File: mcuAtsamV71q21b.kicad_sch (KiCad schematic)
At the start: 29 parts, among them J2 TC2050, U1 ATSAMV71Q21B-A, Y2 12MHz, Y3 CM8V-T1A0.332.768KHZ4PF+_-20P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

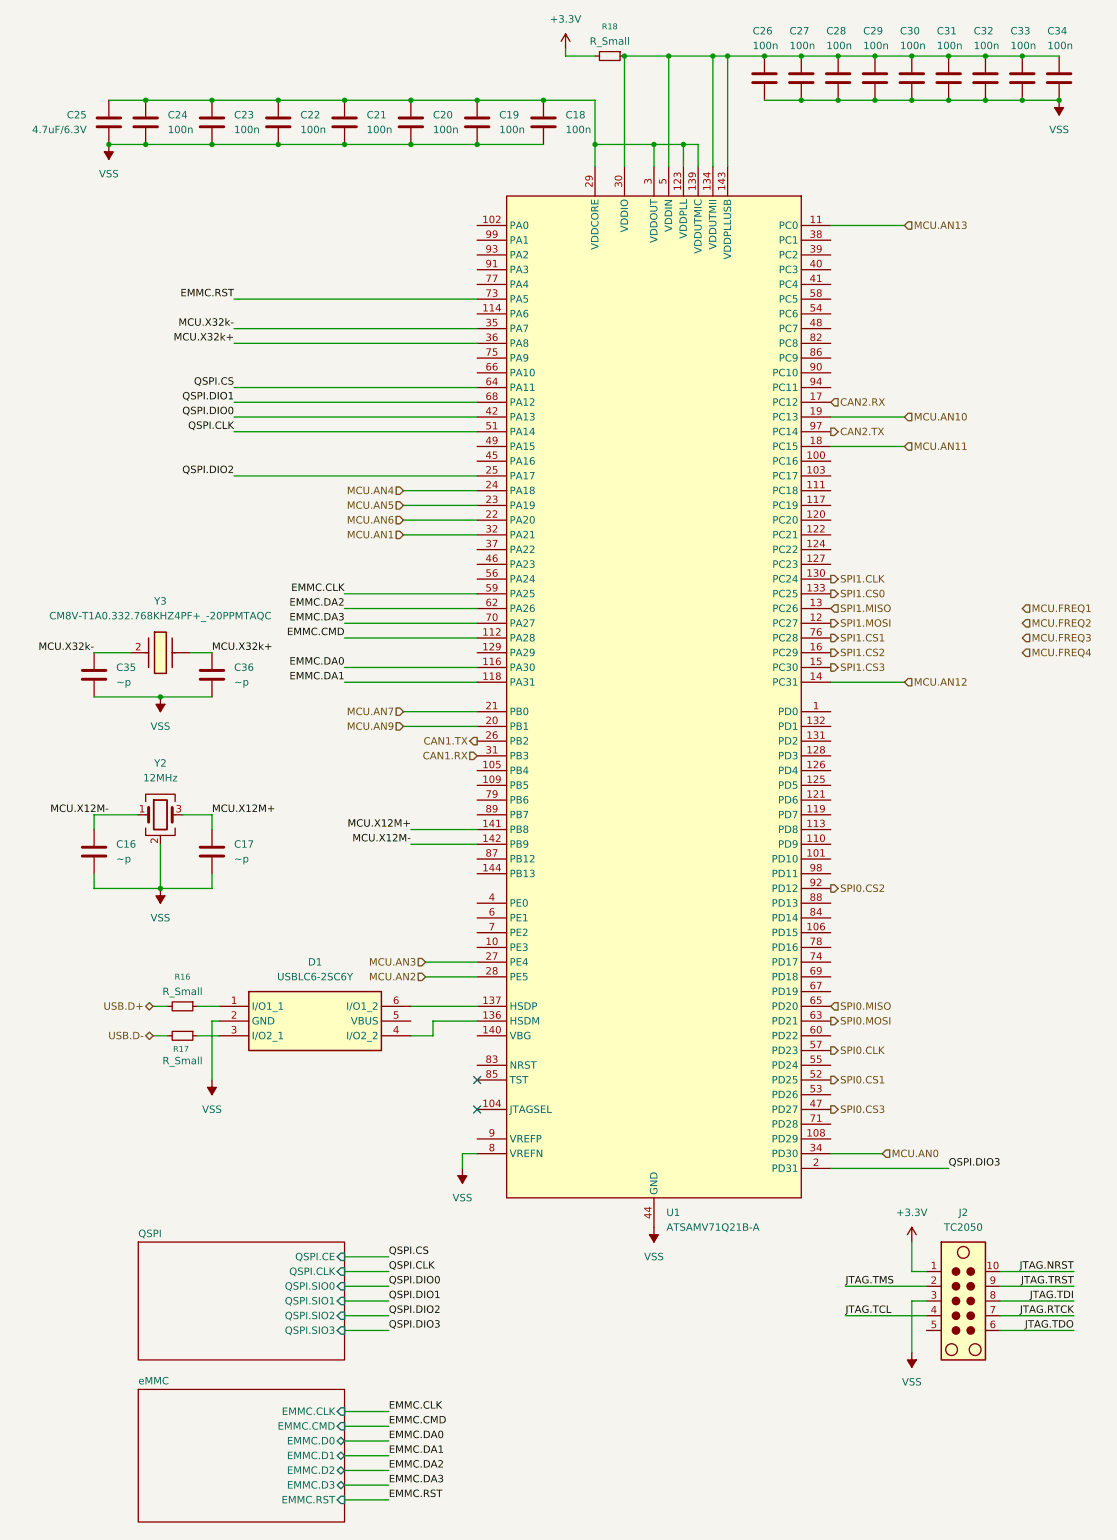
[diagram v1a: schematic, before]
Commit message: Added Wakeup, supply, more pins on MCU
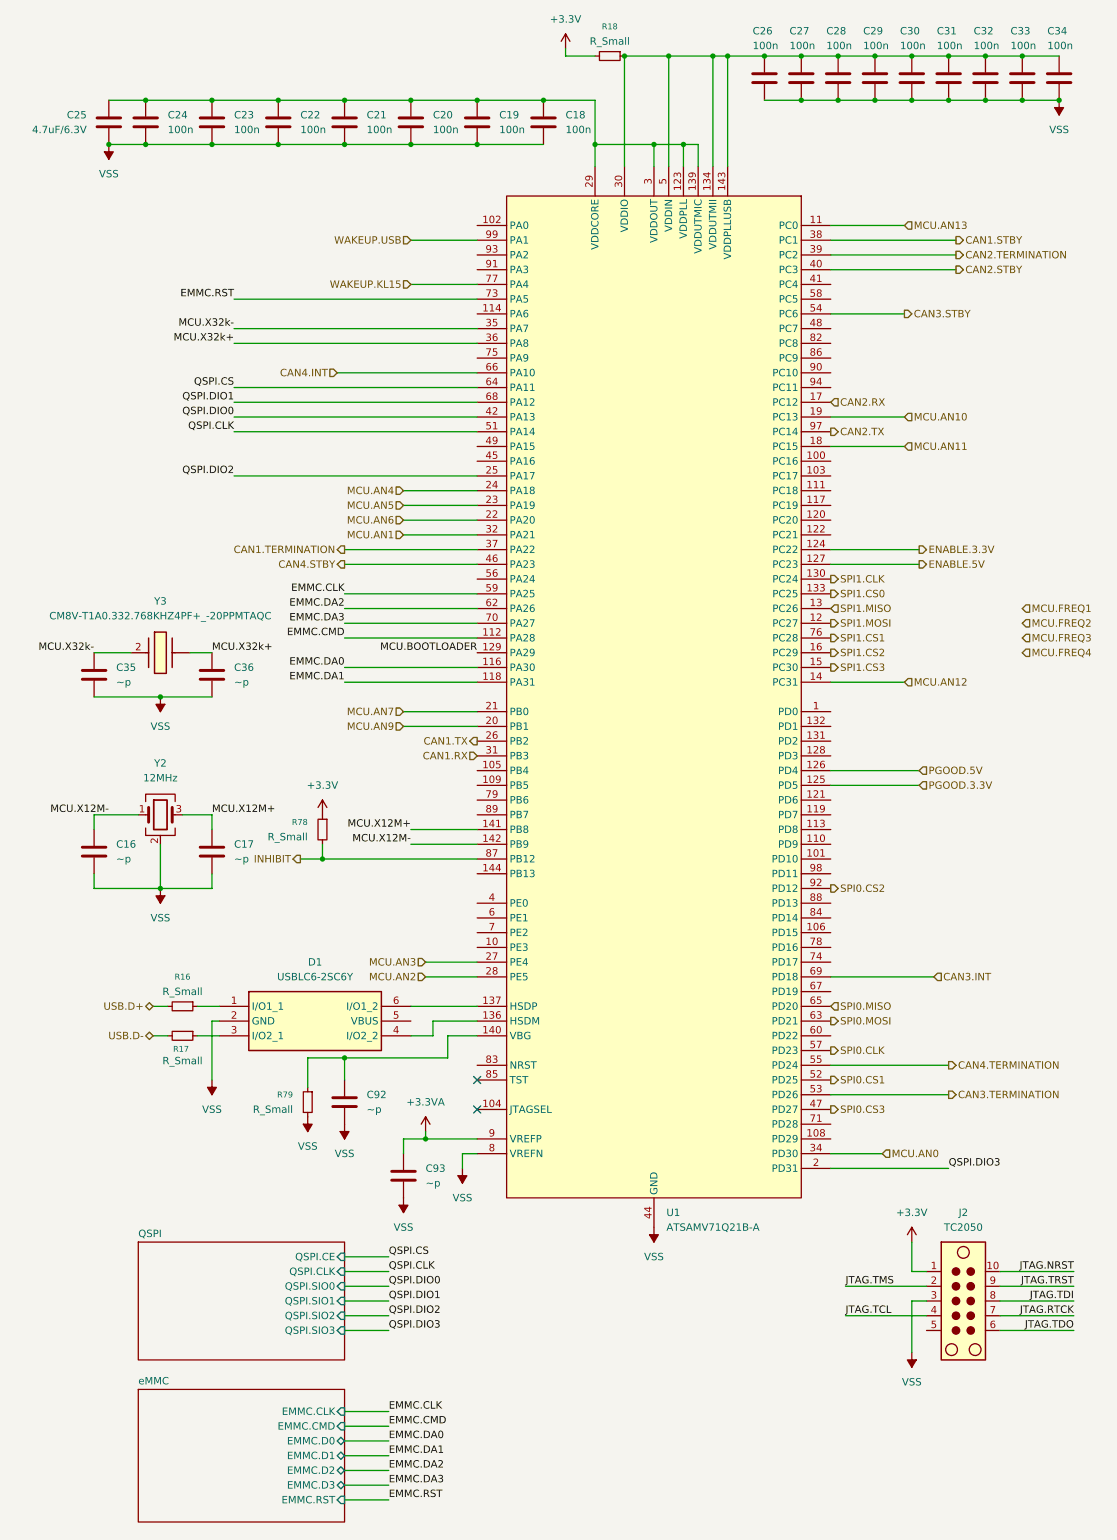
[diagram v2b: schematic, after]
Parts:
- added C92, C93: ~p, Capacitor_SMD:C_0603_1608Metric, symbol Device:C
- added R78, R79: R_Small, Resistor_SMD:R_0603_1608Metric, symbol Device:R_Small
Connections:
- net +3.3V: now also R78.1
- net VSS: now also C92.2, C93.2, R79.2
- net ENABLE.3.3V: now reaches U1.124 (PC22)
- net PGOOD.3.3V: now reaches U1.125 (PD5)
- net PGOOD.5V: now reaches U1.126 (PD4)
- net ENABLE.5V: now reaches U1.127 (PC23)
- net MCU.BOOTLOADER: now reaches U1.129 (PA29)
- net at U1.140 (VBG): now also C92.1, R79.1
- net CAN1.TERMINATION: now reaches U1.37 (PA22)
- net CAN1.STBY: now reaches U1.38 (PC1)
- net CAN2.TERMINATION: now reaches U1.39 (PC2)
- net CAN2.STBY: now reaches U1.40 (PC3)
- net CAN4.STBY: now reaches U1.46 (PA23)
- net CAN3.TERMINATION: now reaches U1.53 (PD26)
- net CAN3.STBY: now reaches U1.54 (PC6)
- net CAN4.TERMINATION: now reaches U1.55 (PD24)
- net CAN4.INT: now reaches U1.66 (PA10)
- net CAN3.INT: now reaches U1.69 (PD18)
- net WAKEUP.KL15: now reaches U1.77 (PA4)
- net INHIBIT: now reaches U1.87 (PB12)
- net INHIBIT: now also R78.2
- net +3.3VA: now reaches U1.9 (VREFP)
- net +3.3VA: now also C93.1
- net WAKEUP.USB: now reaches U1.99 (PA1)

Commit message: Added routing for Freq Inputs
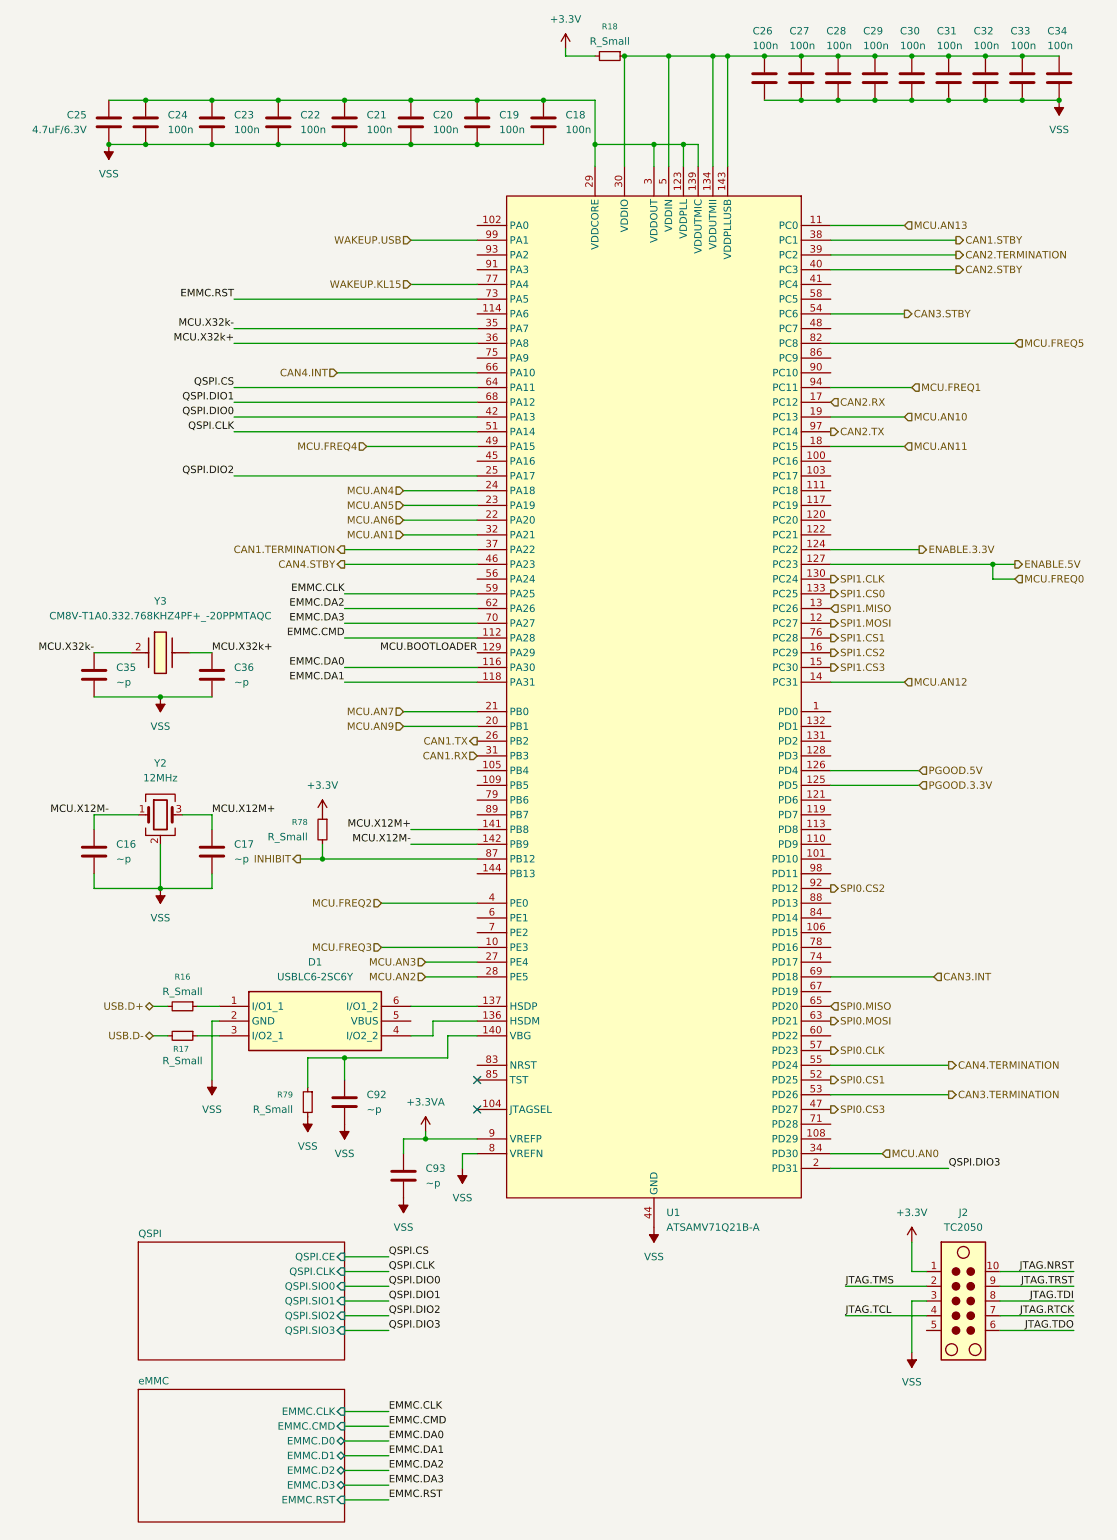
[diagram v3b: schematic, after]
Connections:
- net MCU.FREQ1: now also U1.94 (PC11)
- net MCU.FREQ2: now also U1.4 (PE0)
- net MCU.FREQ3: now also U1.10 (PE3)
- net MCU.FREQ4: now also U1.49 (PA15)
- net MCU.FREQ5: now reaches U1.82 (PC8)
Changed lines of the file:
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@@
+	)
+	(junction
+		(at 177.8 111.76)
+		(diameter 0)
+		(color 0 0 0 0)
 	)
 	(junction
@@
 	(wire
 		(pts
+			(xy 177.8 114.3) (xy 177.8 111.76)
+		)
+		(stroke
+			(width 0)
+			(type default)
+		)
+	)
+	(wire
+		(pts
 			(xy 144.78 31.75) (xy 151.13 31.75)
 		)
@@
 	(wire
 		(pts
+			(xy 181.61 114.3) (xy 177.8 114.3)
+		)
+		(stroke
+			(width 0)
+			(type default)
+		)
+	)
+	(wire
+		(pts
 			(xy 77.47 157.48) (xy 88.9 157.48)
 		)
@@
 	(wire
 		(pts
+			(xy 177.8 111.76) (xy 181.61 111.76)
+		)
+		(stroke
+			(width 0)
+			(type default)
+		)
+	)
+	(wire
+		(pts
 			(xy 77.47 31.75) (xy 88.9 31.75)
 		)
@@
 	(wire
 		(pts
-			(xy 149.86 111.76) (xy 165.1 111.76)
+			(xy 149.86 111.76) (xy 177.8 111.76)
 		)
 		(stroke
@@
 	(wire
 		(pts
+			(xy 72.39 170.18) (xy 88.9 170.18)
+		)
+		(stroke
+			(width 0)
+			(type default)
+		)
+	)
+	(wire
+		(pts
 			(xy 80.01 180.34) (xy 88.9 180.34)
 		)
@@
 	(wire
 		(pts
+			(xy 181.61 73.66) (xy 149.86 73.66)
+		)
+		(stroke
+			(width 0)
+			(type default)
+		)
+	)
+	(wire
+		(pts
 			(xy 100.33 31.75) (xy 109.22 31.75)
 		)
@@
 	(wire
 		(pts
+			(xy 69.85 91.44) (xy 88.9 91.44)
+		)
+		(stroke
+			(width 0)
+			(type default)
+		)
+	)
+	(wire
+		(pts
 			(xy 77.47 63.5) (xy 88.9 63.5)
 		)
@@
 	(wire
 		(pts
+			(xy 149.86 81.28) (xy 163.83 81.28)
+		)
+		(stroke
+			(width 0)
+			(type default)
+		)
+	)
+	(wire
+		(pts
 			(xy 170.18 24.13) (xy 176.53 24.13)
 		)
@@
 		(pts
 			(xy 149.86 58.42) (xy 171.45 58.42)
+		)
+		(stroke
+			(width 0)
+			(type default)
+		)
+	)
+	(wire
+		(pts
+			(xy 72.39 177.8) (xy 88.9 177.8)
 		)
 		(stroke
@@
 		)
 	)
+	(hierarchical_label "MCU.FREQ5"
+		(shape input)
+		(at 181.61 73.66 0)
+		(effects
+			(font
+				(size 1.27 1.27)
+			)
+			(justify left)
+		)
+	)
 	(hierarchical_label "MCU.AN0"
 		(shape input)
@@
 	(hierarchical_label "MCU.FREQ2"
 		(shape input)
-		(at 182.88 121.92 0)
-		(effects
-			(font
-				(size 1.27 1.27)
-			)
-			(justify left)
+		(at 72.39 170.18 180)
+		(effects
+			(font
+				(size 1.27 1.27)
+			)
+			(justify right)
 		)
 	)
@@
 	(hierarchical_label "MCU.FREQ1"
 		(shape input)
-		(at 182.88 119.38 0)
+		(at 163.83 81.28 0)
 		(effects
 			(font
@@
 	(hierarchical_label "MCU.FREQ4"
 		(shape input)
-		(at 182.88 127 0)
-		(effects
-			(font
-				(size 1.27 1.27)
-			)
-			(justify left)
+		(at 69.85 91.44 180)
+		(effects
+			(font
+				(size 1.27 1.27)
+			)
+			(justify right)
 		)
 	)
@@
 		)
 	)
+	(hierarchical_label "MCU.FREQ0"
+		(shape input)
+		(at 181.61 114.3 0)
+		(effects
+			(font
+				(size 1.27 1.27)
+			)
+			(justify left)
+		)
+	)
 	(hierarchical_label "CAN2.TERMINATION"
 		(shape output)
@@
 	(hierarchical_label "MCU.FREQ3"
 		(shape input)
-		(at 182.88 124.46 0)
-		(effects
-			(font
-				(size 1.27 1.27)
-			)
-			(justify left)
+		(at 72.39 177.8 180)
+		(effects
+			(font
+				(size 1.27 1.27)
+			)
+			(justify right)
 		)
 	)
@@
 	(hierarchical_label "ENABLE.5V"
 		(shape output)
-		(at 165.1 111.76 0)
-		(effects
-			(font
+		(at 181.61 111.76 0)
+		(effects
+			(font

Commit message: Added missing parts of IOcan schematic
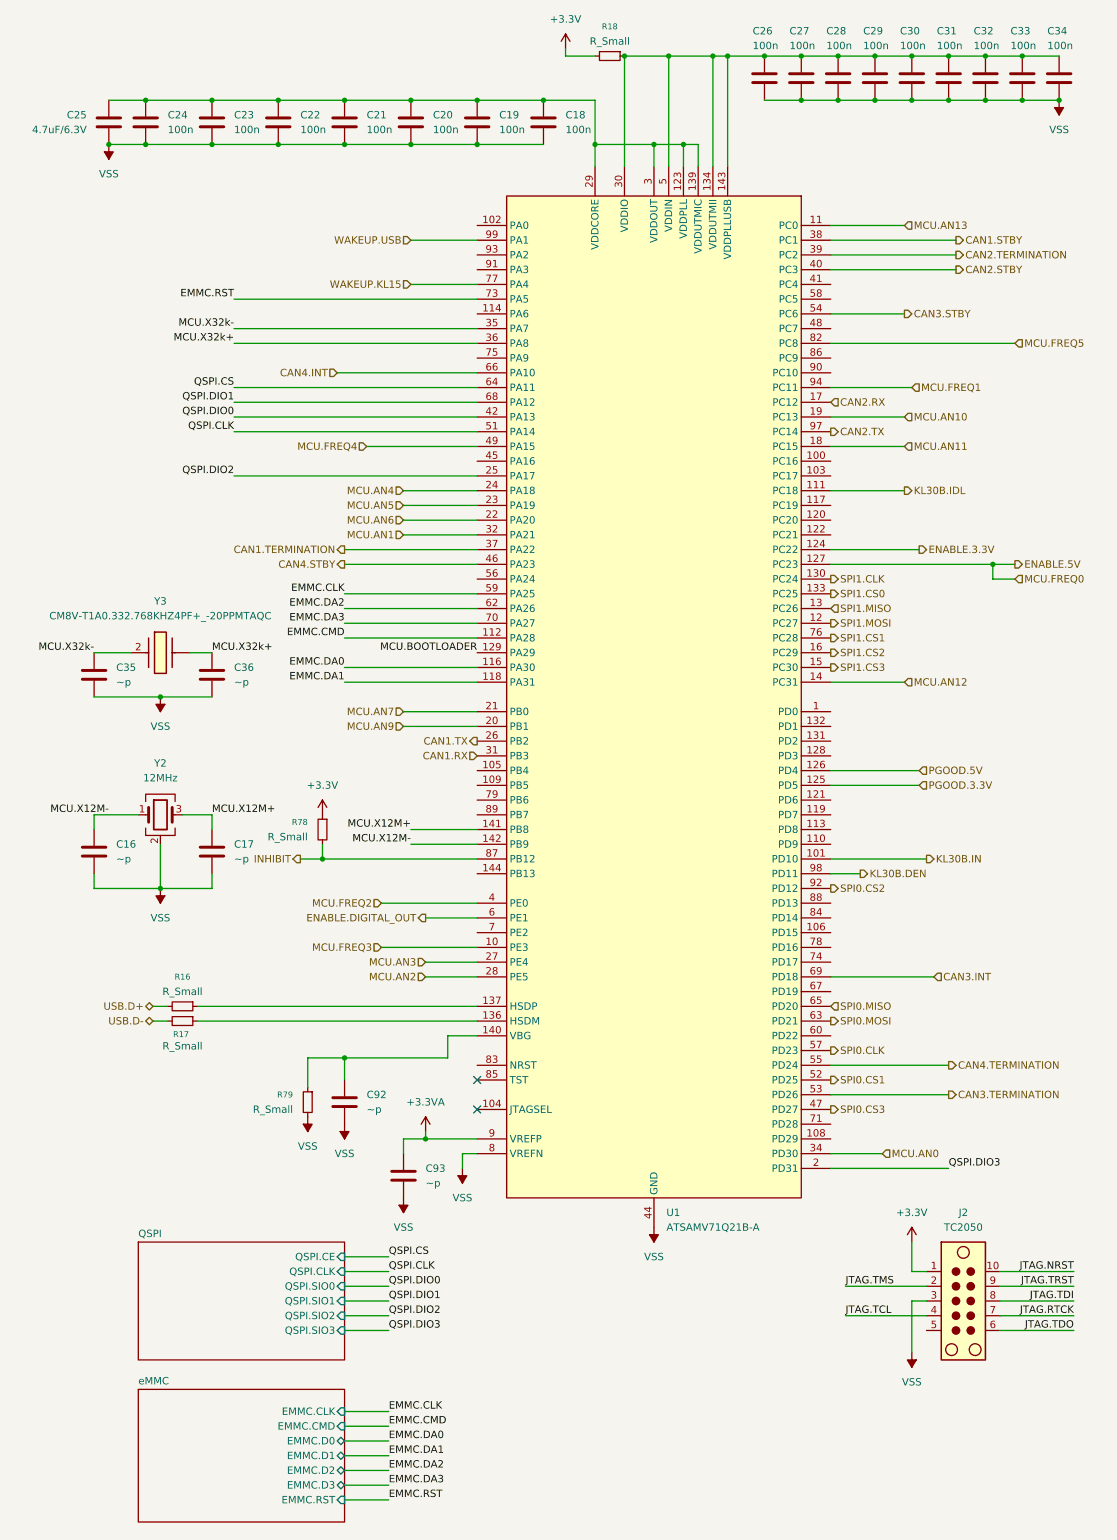
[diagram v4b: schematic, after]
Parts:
- removed D1: USBLC6-2SC6Y, SOT95P280X145-6N, symbol SamacSys_Parts:USBLC6-2SC6Y
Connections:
- net at R16.1: now also U1.137 (HSDP)
- net at R17.1: now also U1.136 (HSDM)
- net KL30B.IN: now reaches U1.101 (PD10)
- net KL30B.IDL: now reaches U1.111 (PC18)
- net ENABLE.DIGITAL_OUT: now reaches U1.6 (PE1)
- net KL30B.DEN: now reaches U1.98 (PD11)
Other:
- moved on the sheet: R17

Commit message: Checked pinouts
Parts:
- C18, C19, C20, C21, C22, C23, C24, C26, C27, C28, C29, C30, C31, C32, C33, C34: value 100n -> 100n/6.3V
- C35, C36: value ~p -> 6pF
- C93: value ~p -> 100nF/6.3V
- R16, R17, R18: value R_Small -> 0R
- R78: value R_Small -> (none); now not fitted
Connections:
- net CAN4.STBY: now also U1.56 (PA24); no longer U1.46 (PA23)
- net SWDIO: now reaches U1.79 (PB6)
- net SWDRST: now reaches U1.83 (NRST)
- net SWCLK: now reaches U1.89 (PB7)
- net MCU.FREQ2 renamed 5V_OUT_ENABLE
- no-connect marks 2 -> 40
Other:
- note added: "IOcan MCU with external components"
- note added: "MCU pinout Checked OK, TagConnect - to check, Analog supply - to check Component values - to check"
- moved on the sheet: C19, C20, C21, C22, C23, C24, C25, C92, R79

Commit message: Updated reverse polarity protection
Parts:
- added C97: 100nF/6.3V, Capacitor_SMD:C_0603_1608Metric, symbol Device:C
- added L3: L_Ferrite_Small, Inductor_SMD:L_0805_2012Metric, symbol Device:L_Ferrite_Small
- added R80: 10k, Resistor_SMD:R_0603_1608Metric, symbol Device:R_Small
- added R85, R86: 0R, Resistor_SMD:R_0603_1608Metric, symbol Device:R_Small
- C92: value ~p -> 10p
- R79: value R_Small -> 5.62k
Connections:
- net +3.3V: now also L3.1
- net +3.3VA: now also L3.2
- net PGOOD.3.3V: now also R85.1, R86.1; no longer U1.125 (PD5)
- net SWDRST: now also C97.1, R80.2, R85.2
- net VSS: now also C97.2
- net MCU_3V3: now reaches C26.1, C27.1, C28.1, C29.1, C30.1, C31.1, C32.1, C33.1, C34.1, R18.1, U1.134 (VDDUTMII), U1.143 (VDDPLLUSB), U1.30 (VDDIO), U1.43 (VDDIO), U1.5 (VDDIN), U1.72 (VDDIO), U1.80 (VDDIO), U1.96 (VDDIO)
- net MCU_3V3: now also R80.1
- new net: R86.2, U1.125 (PD5)
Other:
- moved on the sheet: C93, R18
